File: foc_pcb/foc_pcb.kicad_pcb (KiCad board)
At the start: 2 copper layers, 144.8 x 95.2 mm, 50 parts, among them IC1 AS5600-ASOT, J1 USB_C_Receptacle_USB2.0, J2 Conn_01x03, J3 Conn_01x03, J4 Conn_01x04, J5 XT60PW-M, J6 XT60PW-M, J7 Conn_01x02, J8 Conn_01x02, J9 Conn_01x02, SW1 SW_Push, U1 DRV8313PWPR, U2 ATMEGA328P-AU, U3 LM2596S-5, U5 CH340C, Y1 ABM3-16MHZ

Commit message: added motor mount
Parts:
- removed C15: 100nF, Capacitor_SMD:C_0603_1608Metric
- removed L1: 47uH, SPM6530T-R47M170:IND_SPM6530T-R47M170
- removed U3: LM2596S-5, Package_TO_SOT_SMD:TO-263-5_TabPin3
- added H1: motorMount, MountingHole:MountingHole_3.2mm_M3, F.Cu at (294.6, 167.6)
- added H2: motorMount, MountingHole:MountingHole_3.2mm_M3, F.Cu at (252.6, 209.6)
- added H3: motorMount, MountingHole:MountingHole_3.2mm_M3, F.Cu at (294.6, 251.5)
- added H4: motorMount, MountingHole:MountingHole_3.2mm_M3, F.Cu at (336.5, 209.6)
- added J10: Conn_02x03_Top_Bottom, Connector_PinHeader_2.54mm:PinHeader_2x03_P2.54mm_Vertical, F.Cu at (182.9, 154.9)
- added R13: 200, Resistor_SMD:R_0603_1608Metric, F.Cu at (150.3, 78.8)
- added R14: 590, Resistor_SMD:R_0603_1608Metric, F.Cu at (150.3, 81.3)
- added VR1: LM317LCPK, LM317LCPK:VREG_LM317LCPK, F.Cu at (143.5, 137.2)
- C4: value 220uF -> .1uF
- C5: value 680uF -> 1uF
- D2: value SK32 -> 1N5819HW-7-F; footprint SK32WA:SOD-123F_L2.8-W1.8-LS3.7-RD -> 1N5819HW-7-F:SOD3715X145N
- moved C14 226.7 mm to (285.0, 210.8), turned to 180 degrees
- moved IC1 186.4 mm to (294.6, 209.6)
- moved R9 182.8 mm to (302.3, 205.7), turned to -90 degrees
- moved R11 161.0 mm to (306.1, 205.7), turned to -90 degrees
- moved J3 151.9 mm to (198.1, 147.3)
- moved J2 141.1 mm to (198.1, 134.6)
- moved J8 133.8 mm to (198.1, 114.3), turned to 0 degrees
- moved J7 133.3 mm to (198.1, 108.0)
- moved J9 132.4 mm to (198.1, 124.5), turned to 0 degrees
- moved C13 122.2 mm to (285.0, 207.0), turned to 180 degrees
- moved J4 117.1 mm to (182.9, 105.4), turned to 90 degrees
- moved C12 113.9 mm to (142.2, 76.3)
- moved R3 110.0 mm to (146.2, 73.8)
- moved C1 109.0 mm to (138.2, 71.3)
- moved U1 100.2 mm to (186.7, 142.9)
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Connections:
- C4 pad 1: +5V -> VCC
- C5 pad 1: VCC -> +5V
- J1 pad A4: VCC -> +5V
- J1 pad A9: VCC -> +5V
- J1 pad B4: VCC -> +5V
- J1 pad B9: VCC -> +5V
- J1 pad S1: GND -> unconnected-(J1-SHIELD-PadS1)_1
- U2 pad 15: /aTX2 -> /mosi
- U2 pad 16: unconnected-(U2-PB4-Pad16) -> /miso
- U2 pad 32: unconnected-(U2-PD2-Pad32) -> /aTX2
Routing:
- net /esda: track 0.00 -> 10.3 mm
- net +5V: track 0.00 -> 10.2 mm
- net Net-(IC1-VDD3V3): track 0.00 -> 6.89 mm
- net /escl: track 0.00 -> 5.98 mm
- net GND: track 0.00 -> 3.81 mm
- net /ud-: track 0.97 -> 0.00 mm
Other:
- board size 144.8 x 95.2 mm -> 320 x 243.8 mm

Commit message: added level shifter, layout done
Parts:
- added H5: motorMount, MountingHole:MountingHole_3.2mm_M3, F.Cu at (324.2, 179.9)
- added H6: motorMount, MountingHole:MountingHole_3.2mm_M3, F.Cu at (264.9, 179.9)
- added H7: motorMount, MountingHole:MountingHole_3.2mm_M3, F.Cu at (264.9, 239.2)
- added H8: motorMount, MountingHole:MountingHole_3.2mm_M3, F.Cu at (324.2, 239.2)
- added J11: Conn_01x03, Connector_PinHeader_2.54mm:PinHeader_1x03_P2.54mm_Vertical, F.Cu at (341.6, 297.2)
- added R15: 10k, Resistor_SMD:R_0603_1608Metric, B.Cu at (333.6, 283.2)
- added R16: 10k, Resistor_SMD:R_0603_1608Metric, B.Cu at (338.6, 278.1)
- added R17: 10k, Resistor_SMD:R_0603_1608Metric, B.Cu at (333.6, 278.1)
- added R18: 10k, Resistor_SMD:R_0603_1608Metric, B.Cu at (338.6, 283.2)
- added U3: BSS138, BSS138-7-F:SOT95P240X110-3N, F.Cu at (340.6, 289.6)
- added U4: BSS138, BSS138-7-F:SOT95P240X110-3N, F.Cu at (347.0, 289.6)
- C1, C10, C12, C16, C17, C2, C3, C4, C5, C6, C7, C8, C9, R1, R10, R12, R13, R14, R2, R3, R4, R5, R6, R7, R8: moved to B.Cu
- D1: value 19-213/Y2C-CQ2R2L/3T(CY) -> simpleFOCled
- moved SW1 313.8 mm to (364.5, 264.2), turned to -90 degrees
- moved C9 305.7 mm to (364.5, 281.2), turned to -90 degrees
- moved C12 292.0 mm to (350.9, 280.7)
- moved C10 291.6 mm to (350.9, 277.5), turned to 180 degrees
- moved R5 290.2 mm to (364.5, 270.1), turned to -90 degrees
- moved R6 281.4 mm to (353.1, 272.2), turned to 90 degrees
- moved R10 280.5 mm to (355.2, 262.9), turned to 180 degrees
- moved J1 278.9 mm to (361.4, 298.6)
- moved R7 277.9 mm to (350.5, 272.2), turned to -90 degrees
- moved C5 273.6 mm to (337.0, 269.2), turned to 180 degrees
- moved U2 273.3 mm to (348.0, 229.9)
- moved U5 272.9 mm to (356.8, 280.0)
- moved C4 271.6 mm to (332.0, 269.2), turned to 180 degrees
- moved R8 270.3 mm to (355.2, 257.8), turned to 180 degrees
- moved C1 268.6 mm to (302.3, 284.0), turned to 90 degrees
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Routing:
- net GND: track 3.81 -> 87.6 mm
- net /rst: track 0.00 -> 69.7 mm, vias 0 -> 2
- net +5V: track 10.2 -> 61.7 mm, vias 0 -> 3
- net +3.3V: track 0.00 -> 38.4 mm, vias 0 -> 1
- net /fault: track 0.00 -> 29.0 mm, vias 0 -> 1
- net /nSlp: track 0.00 -> 28.2 mm, vias 0 -> 1
- net /nRes: track 0.00 -> 27.6 mm, vias 0 -> 1
- net /ud+: track 0.00 -> 21.0 mm
- net /en: track 0.00 -> 20.1 mm, vias 0 -> 3
- net /ud-: track 0.00 -> 18.7 mm
- net /3vin: track 0.00 -> 17.9 mm
- net /x1: track 0.00 -> 17.8 mm, vias 0 -> 1
- net /x2: track 0.00 -> 14.4 mm, vias 0 -> 1
- net VCC: track 0.00 -> 12.3 mm
- net /lvTX: track 0.00 -> 9.90 mm
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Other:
- board outline removed

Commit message: backup in case footprint swap fails
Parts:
- moved R4 80.0 mm to (355.2, 268.0)
- moved R13 19.4 mm to (338.3, 259.1)
- moved R17 19.4 mm to (350.5, 287.5), turned to -90 degrees
- moved R14 12.0 mm to (333.2, 259.1)
- moved R16 9.37 mm to (337.8, 287.5), turned to -90 degrees
- moved C3 7.51 mm to (290.8, 275.6), turned to -90 degrees
- moved C2 7.45 mm to (290.8, 272.6), turned to -90 degrees
- moved R18 7.33 mm to (344.6, 287.5), turned to -90 degrees
- moved R15 4.77 mm to (335.7, 287.5), turned to -90 degrees
- turned R8 to 0 degrees
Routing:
- net +5V: track 61.7 -> 320.9 mm, vias 3 -> 9
- net /sck: track 0.00 -> 136.6 mm, vias 0 -> 3
- net /mosi: track 0.00 -> 129.6 mm, vias 0 -> 3
- net VCC: track 12.3 -> 140.2 mm, vias 0 -> 3
- net /miso: track 0.00 -> 122.6 mm, vias 0 -> 3
- net /rst: track 69.7 -> 168.6 mm
- net /aRX1: track 0.00 -> 93.7 mm, vias 0 -> 2
- net /aTX1: track 0.00 -> 88.7 mm, vias 0 -> 2
- net GND: track 87.6 -> 0.58 mm
- net /in3: track 0.00 -> 65.3 mm
- net /in1: track 0.00 -> 64.4 mm
- net /in2: track 0.00 -> 64.3 mm
- net /escl: track 5.98 -> 63.5 mm, vias 0 -> 2
- net /esda: track 10.3 -> 64.8 mm, vias 0 -> 2
- net /out1: track 0.00 -> 53.6 mm, vias 0 -> 2
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- added copper zone on B.Cu, net GND
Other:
- rule pad_to_mask_clearance: 0 -> 0.038

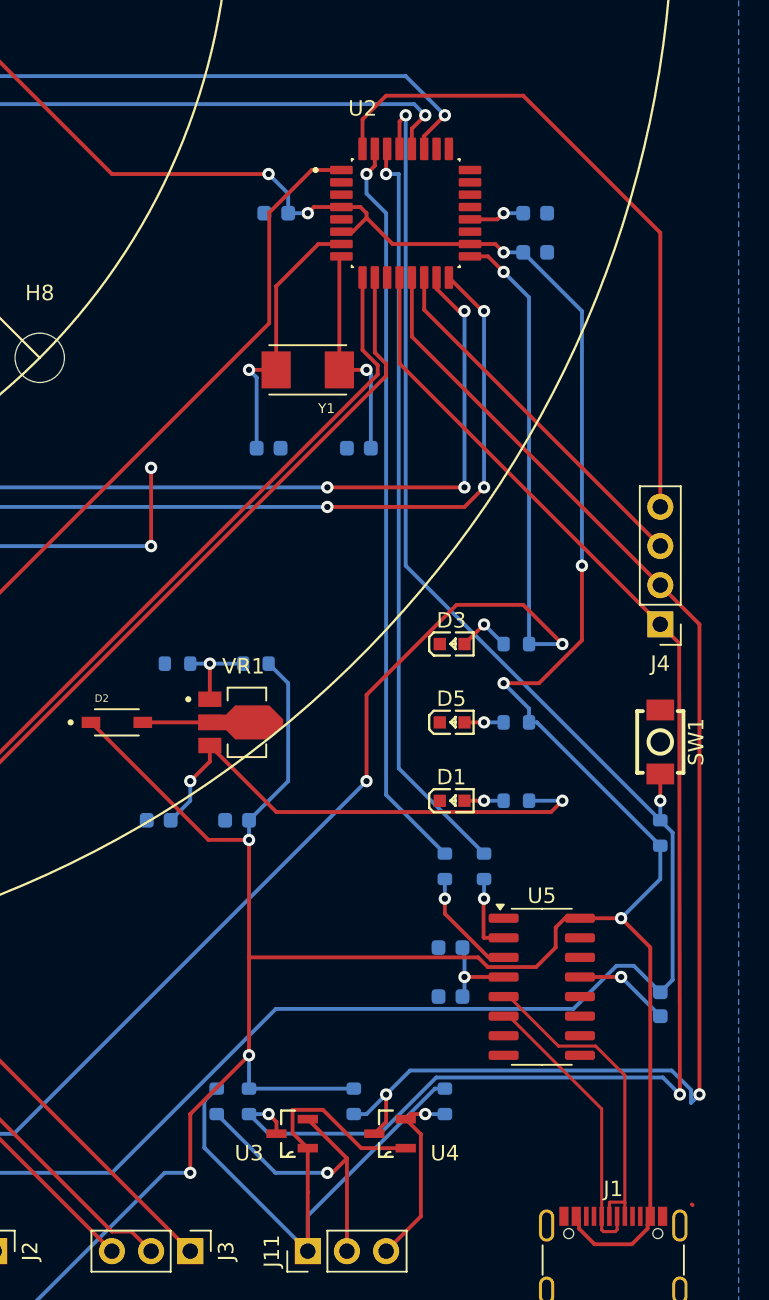
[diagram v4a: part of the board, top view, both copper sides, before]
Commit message: swapped footprint, fixed several DRC violations
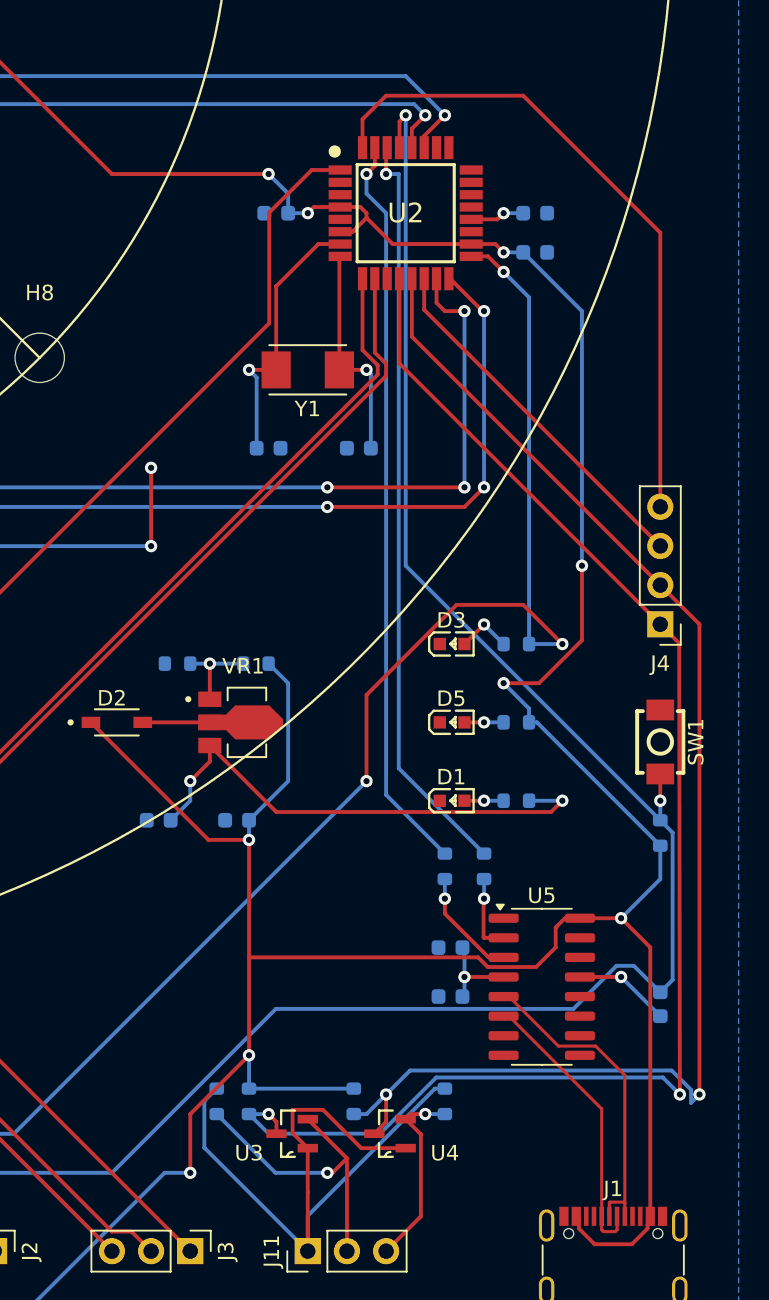
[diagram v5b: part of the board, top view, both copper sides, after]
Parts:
- D1: value simpleFOCled -> 19-213/Y2C-CQ2R2L/3T(CY)
- U2: footprint ATMEGA328P-AU:QFP80P900X900X120-32N -> ATMEGA328P-AU-NEW:QFP80P900X900X120-32N
- U3, U4: value BSS138 -> BSS138-7-F
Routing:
- net /mosi: track 129.6 -> 130.1 mm

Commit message: added thicker tracks for vcc
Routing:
- net GND: track 0.51 -> 70.4 mm, vias 0 -> 14
- net VCC: track 140.2 -> 108.2 mm, vias 3 -> 4
- net /out1: track 53.6 -> 26.4 mm
- net Net-(U2-PD7): track 51.4 -> 75.5 mm, vias 2 -> 3
- net /out2: track 47.4 -> 26.4 mm
- net /out3: track 44.6 -> 25.9 mm
- net +5V: track 320.9 -> 318.8 mm
- net Net-(U1-CPL): track 6.08 -> 7.14 mm
- net Net-(U1-CPH): track 6.13 -> 6.99 mm

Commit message: before switch usb
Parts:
- U1: footprint DRV8313PWPR:SOP65P640X120-29N -> DRV8313PWPR:HTSSOP-28_L9.8-W4.5-P0.65-LS6.6-BL-EP
- moved C2 3.59 mm to (293.4, 270.0)
- moved C3 3.03 mm to (290.8, 272.6)
- turned U1 to -90 degrees
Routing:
- net VCC: track 108.2 -> 35.5 mm, vias 4 -> 6
- net /out1: track 26.4 -> 67.4 mm
- net /out2: track 26.4 -> 61.3 mm
- net /out3: track 25.9 -> 52.3 mm
- net GND: track 70.4 -> 76.5 mm, vias 14 -> 22
- net Net-(U1-CPH): track 6.99 -> 4.26 mm
- net Net-(U1-CPL): track 7.14 -> 4.63 mm
- net /nSlp: track 28.2 -> 30.2 mm
- net /miso: track 122.6 -> 123.8 mm
- net /mosi: track 130.1 -> 131.2 mm
- net /sck: track 136.6 -> 137.6 mm
- net /nRes: track 27.6 -> 28.3 mm
- added copper zone on F.Cu, net VCC
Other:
- board outline added: 156.2 x 162.6 mm
- rule pad_to_mask_clearance: 0.038 -> 0
